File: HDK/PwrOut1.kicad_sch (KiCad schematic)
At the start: 10 parts, among them J201 PwrOut_{1}, J202 PwrOut_{1}, J203 PwrOut_{1}, J204 PwrOut_{1}, J205 PwrOut_{1}, J206 PwrOut_{1}, J207 PwrOut_{1}, J208 PwrOut_{1}, J209 PwrOut_{1}, J210 PwrOut_{1}

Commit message: updated sch
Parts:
- removed J207, J208, J209, J210: PwrOut_{1}, Connector_Molex:Molex_Mini-Fit_Jr_5566-02A_2x01_P4.20mm_Vertical, symbol Connector_Generic:Conn_01x02
- added C201, C202, C203, C204, C205, C206: 470u, Capacitor_THT:CP_Radial_D10.0mm_P5.00mm, symbol Device:C_Polarized
- added D201, D202, D203, D204, D205, D206, D207, D208, D209, D210, D211, D212: D_TVS, Diode_SMD:D_SMA, symbol Device:D_TVS
- J201, J202, J203, J204, J205, J206: value PwrOut_{1} -> P1-Out; footprint Connector_Molex:Molex_Mini-Fit_Jr_5566-02A_2x01_P4.20mm_Vertical -> Connector_AMASS:AMASS_XT30U-M_1x02_P5.0mm_Vertical
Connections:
- net GND: now also C201.2, C202.2, C203.2, C204.2, C205.2, C206.2, D201.1 (A1), D202.1 (A1), D203.1 (A1), D204.1 (A1), D205.1 (A1), D206.1 (A1), D207.1 (A1), D208.1 (A1), D209.1 (A1), D210.1 (A1), D211.1 (A1), D212.1 (A1)
- net VCCF_{1} renamed VCCF_{Sec}
- net VCCF_{Sec}: now also C201.1, C202.1, C203.1, C204.1, C205.1, C206.1, D201.2 (A2), D202.2 (A2), D203.2 (A2), D204.2 (A2), D205.2 (A2), D206.2 (A2), D207.2 (A2), D208.2 (A2), D209.2 (A2), D210.2 (A2), D211.2 (A2), D212.2 (A2)
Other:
- note added: "Power 1-Out connectors: (XT30) Currect Max: 30A (Cont) Power 1-Out Ports: - 6x Thrusters (Propulsion) - 4x Add-Ons Features: - TVS Protection for Surge Protection - High Powered Capacitor for Sudden Voltage Drop Protection Potential Features: - Individual Fuse per ESC - Slots for Buck Convertors for servo voltages"
- note removed: "PwrOut connectors: (XT60) Currect Max: 30A (Cont) Pwr1 Out: - 6x Thrusters (Propulsion) - 4x Add-Ons Potential Feature: - Individual Fuse per ESC - Slots for Buck Convertors for servo voltages"

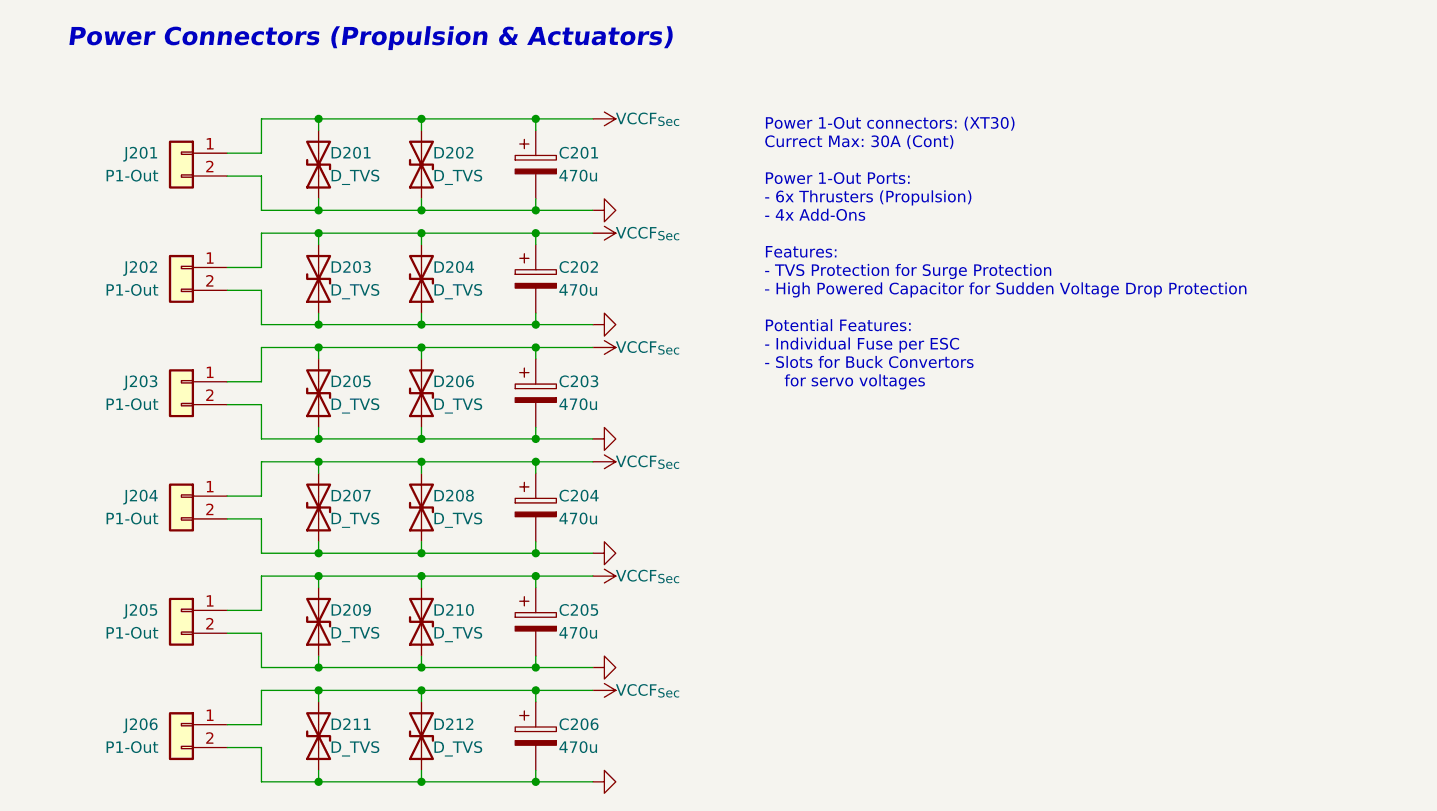
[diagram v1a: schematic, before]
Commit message: added connectors
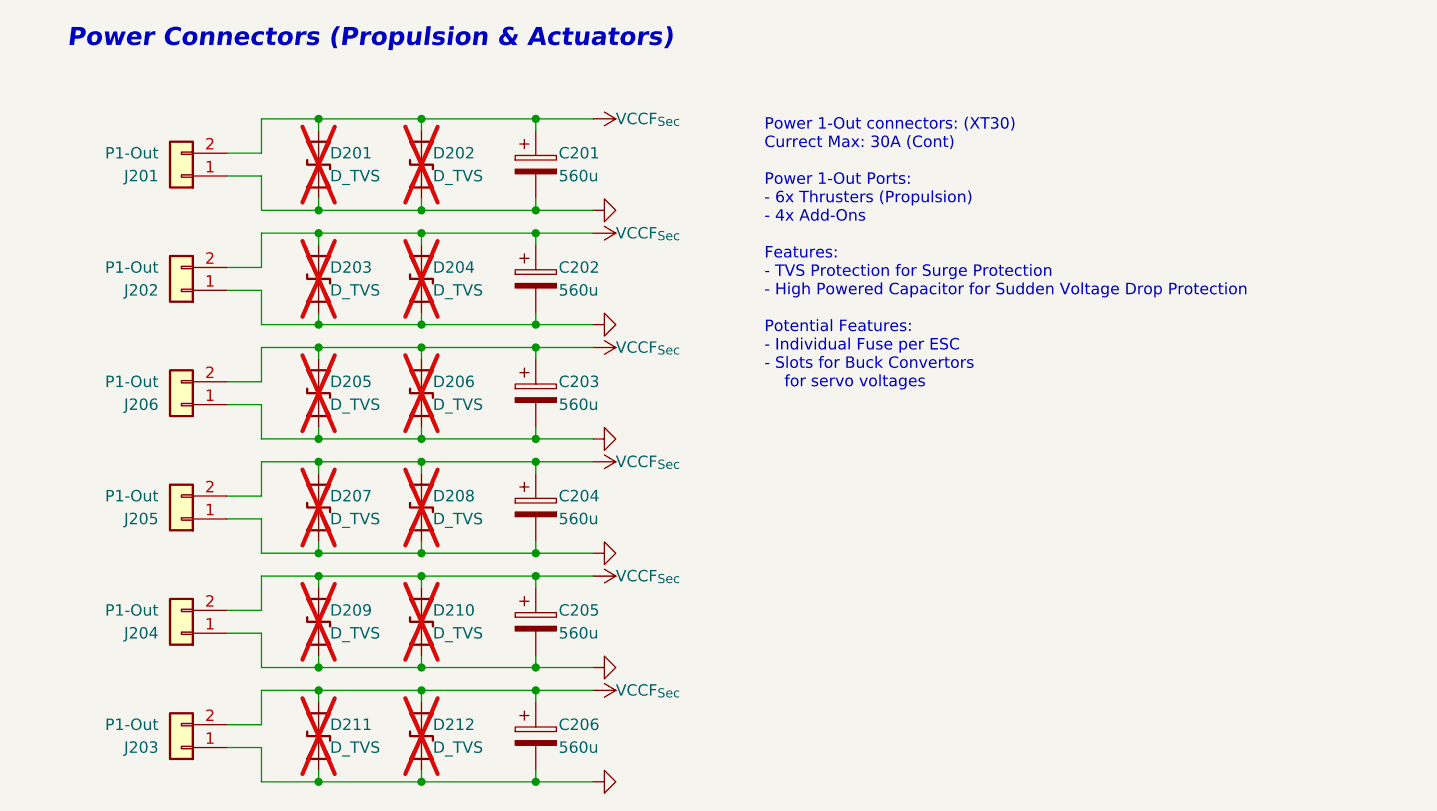
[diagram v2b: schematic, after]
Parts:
- C201, C202, C203, C204, C205, C206: value 470u -> 560u
- D201, D202, D203, D204, D205, D206, D207, D208, D209, D210, D211, D212: footprint Diode_SMD:D_SMA -> (none); now not fitted
- J201, J202, J203, J204, J205, J206: footprint Connector_AMASS:AMASS_XT30U-M_1x02_P5.0mm_Vertical -> mecatron-kicad-footprints:AMASS_XT30PW-F_1x02_P2.50mm_Horizontal
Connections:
- net GND: now also J201.1 (Pin_1), J202.1 (Pin_1), J203.1 (Pin_1), J204.1 (Pin_1), J205.1 (Pin_1), J206.1 (Pin_1); no longer J201.2 (Pin_2), J202.2 (Pin_2), J203.2 (Pin_2), J204.2 (Pin_2), J205.2 (Pin_2), J206.2 (Pin_2)
- net VCCF_{Sec}: now also J201.2 (Pin_2), J202.2 (Pin_2), J203.2 (Pin_2), J204.2 (Pin_2), J205.2 (Pin_2), J206.2 (Pin_2); no longer J201.1 (Pin_1), J202.1 (Pin_1), J203.1 (Pin_1), J204.1 (Pin_1), J205.1 (Pin_1), J206.1 (Pin_1)
